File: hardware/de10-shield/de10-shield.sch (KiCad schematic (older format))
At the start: 35 parts, among them J1 GPIO_0, J10 SW3, J11 SW4, J12 SW5, J13 SW6, J14 SW7, J15 GPIO_0_AUX, J16 GPIO_1_AUX, J17 TFT_DISPLAY, J18 LED_0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

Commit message: done
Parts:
- removed J15: GPIO_0_AUX, Connector_PinSocket_2.54mm:PinSocket_1x20_P2.54mm_Vertical, symbol Connector:Conn_01x20_Female
- added H5, H6: MountingHole_Pad, MountingHole:MountingHole_3.2mm_M3_DIN965_Pad, symbol Mechanical:MountingHole_Pad
- added J15: ENCODER_0, Connector_PinSocket_2.54mm:PinSocket_1x05_P2.54mm_Vertical, symbol Connector:Conn_01x05_Female
- added J20: 5V, Connector_PinHeader_2.54mm:PinHeader_1x02_P2.54mm_Vertical, symbol Connector:Conn_01x02_Female
- added J21: 3.3V, Connector_PinHeader_2.54mm:PinHeader_1x02_P2.54mm_Vertical, symbol Connector:Conn_01x02_Female
- added J22: ENCODER_1, Connector_PinSocket_2.54mm:PinSocket_1x05_P2.54mm_Vertical, symbol Connector:Conn_01x05_Female
- added J23: ENCODER_2, Connector_PinSocket_2.54mm:PinSocket_1x05_P2.54mm_Vertical, symbol Connector:Conn_01x05_Female
- added J24: ENCODER_3, Connector_PinSocket_2.54mm:PinSocket_1x05_P2.54mm_Vertical, symbol Connector:Conn_01x05_Female
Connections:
- net +3V3: now also J15.1 (Pin_1), J21.2 (Pin_2), J22.1 (Pin_1), J23.1 (Pin_1), J24.1 (Pin_1); no longer J2.29 (Pin_29)
- net +5V: now also J20.2 (Pin_2); no longer J1.11 (Pin_11)
- net DIR_0: now also J1.10 (Pin_10); no longer J1.21 (Pin_21)
- net EN_0: now also J1.2 (Pin_2); no longer J1.13 (Pin_13)
- net GND: now also H5.1, J15.2 (Pin_2), J20.1 (Pin_1), J21.1 (Pin_1), J22.2 (Pin_2), J23.2 (Pin_2), J24.2 (Pin_2); no longer J1.12 (Pin_12), J1.30 (Pin_30), J16.15 (Pin_15), J16.6 (Pin_6), J2.12 (Pin_12), J2.30 (Pin_30)
- net MS1_0: now also J1.4 (Pin_4); no longer J1.15 (Pin_15)
- net MS2_0: now also J1.6 (Pin_6); no longer J1.17 (Pin_17)
- net STEP_0: now also J1.8 (Pin_8); no longer J1.19 (Pin_19)
- net VMEM: now also H6.1
- net I_3: now reaches J1.16 (Pin_16)
- net I_3: now also J24.5 (Pin_5)
- net B_3: now reaches J1.18 (Pin_18)
- net B_3: now also J24.4 (Pin_4)
- net A_3: now reaches J1.20 (Pin_20)
- net A_3: now also J24.3 (Pin_3)
- net I_2: now reaches J1.22 (Pin_22)
- net I_2: now also J23.5 (Pin_5)
- net B_2: now reaches J1.24 (Pin_24)
- net B_2: now also J23.4 (Pin_4)
- net A_2: now reaches J1.26 (Pin_26)
- net A_2: now also J23.3 (Pin_3)
- net I_1: now reaches J1.28 (Pin_28)
- net I_1: now also J22.5 (Pin_5)
- net B_1: now reaches J1.32 (Pin_32)
- net B_1: now also J22.4 (Pin_4)
- net A_1: now reaches J1.34 (Pin_34)
- net A_1: now also J22.3 (Pin_3)
- net I_0: now reaches J1.36 (Pin_36)
- net I_0: now also J15.5 (Pin_5)
- net B_0: now reaches J1.38 (Pin_38)
- net B_0: now also J15.4 (Pin_4)
- net A_0: now reaches J1.40 (Pin_40)
- net A_0: now also J15.3 (Pin_3)
- new net: J16.6 (Pin_6), J2.12 (Pin_12)
- new net: J16.15 (Pin_15), J2.30 (Pin_30)
- no-connect marks 2 -> 12

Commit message: done and ordered
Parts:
- added H7: MountingHole_Pad, MountingHole:MountingHole_3.2mm_M3_DIN965_Pad, symbol Mechanical:MountingHole_Pad
- C13, C14: footprint Capacitor_SMD:C_0603_1608Metric -> Capacitor_SMD:C_1210_3225Metric_Pad1.33x2.70mm_HandSolder
- C15: footprint Capacitor_SMD:C_0402_1005Metric -> Capacitor_SMD:C_0603_1608Metric_Pad1.08x0.95mm_HandSolder
- C16: footprint Capacitor_SMD:C_0402_1005Metric -> Capacitor_SMD:C_0805_2012Metric_Pad1.18x1.45mm_HandSolder
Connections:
- net GND: now also H7.1
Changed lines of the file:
@@
 F 0 "C16" H 4315 5546 50  0000 L CNN
 F 1 "0.1uF" H 4315 5455 50  0000 L CNN
-F 2 "Capacitor_SMD:C_0402_1005Metric" H 4238 5350 50  0001 C CNN
+F 2 "Capacitor_SMD:C_0805_2012Metric_Pad1.18x1.45mm_HandSolder" H 4238 5350 50  0001 C CNN
 F 3 "~" H 4200 5500 50  0001 C CNN
 	1    4200 5500
@@
 F 0 "C14" H 1815 4746 50  0000 L CNN
 F 1 "2.2uF" H 1815 4655 50  0000 L CNN
-F 2 "Capacitor_SMD:C_0603_1608Metric" H 1738 4550 50  0001 C CNN
+F 2 "Capacitor_SMD:C_1210_3225Metric_Pad1.33x2.70mm_HandSolder" H 1738 4550 50  0001 C CNN
 F 3 "~" H 1700 4700 50  0001 C CNN
 	1    1700 4700
@@
 F 0 "C13" H 1615 5546 50  0000 L CNN
 F 1 "2.2uF" H 1615 5455 50  0000 L CNN
-F 2 "Capacitor_SMD:C_0603_1608Metric" H 1538 5350 50  0001 C CNN
+F 2 "Capacitor_SMD:C_1210_3225Metric_Pad1.33x2.70mm_HandSolder" H 1538 5350 50  0001 C CNN
 F 3 "~" H 1500 5500 50  0001 C CNN
 	1    1500 5500
@@
 F 0 "C15" H 2615 6846 50  0000 L CNN
 F 1 "5600pF" H 2615 6755 50  0000 L CNN
-F 2 "Capacitor_SMD:C_0402_1005Metric" H 2538 6650 50  0001 C CNN
+F 2 "Capacitor_SMD:C_0603_1608Metric_Pad1.08x0.95mm_HandSolder" H 2538 6650 50  0001 C CNN
 F 3 "~" H 2500 6800 50  0001 C CNN
 	1    2500 6800
@@
 NoConn ~ 2550 3425
 NoConn ~ 4200 3425
+$Comp
+L Mechanical:MountingHole_Pad H7
+U 1 1 605964B9
+P 9950 3825
+F 0 "H7" H 10050 3874 50  0000 L CNN
+F 1 "MountingHole_Pad" H 10050 3783 50  0000 L CNN
+F 2 "MountingHole:MountingHole_3.2mm_M3_DIN965_Pad" H 9950 3825 50  0001 C CNN
+F 3 "~" H 9950 3825 50  0001 C CNN
+	1    9950 3825
+	1    0    0    -1
+$EndComp
+$Comp
+L power:GND #PWR0104
+U 1 1 605964BF
+P 9950 3925
+F 0 "#PWR0104" H 9950 3675 50  0001 C CNN
+F 1 "GND" V 9955 3797 50  0000 R CNN
+F 2 "" H 9950 3925 50  0001 C CNN
+F 3 "" H 9950 3925 50  0001 C CNN
+	1    9950 3925
+	0    1    1    0
+$EndComp
 $EndSCHEMATC

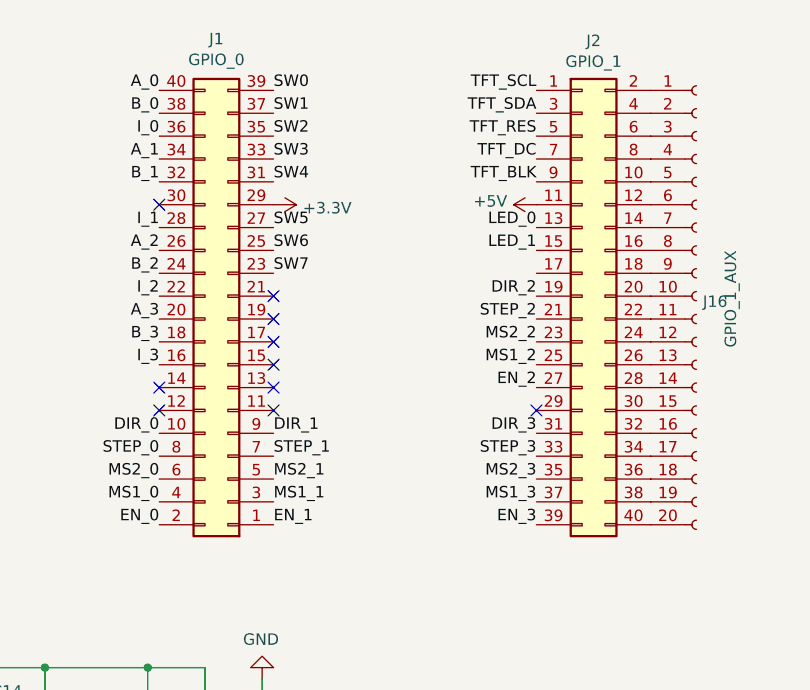
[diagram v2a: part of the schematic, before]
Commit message: with de10 shield pinout
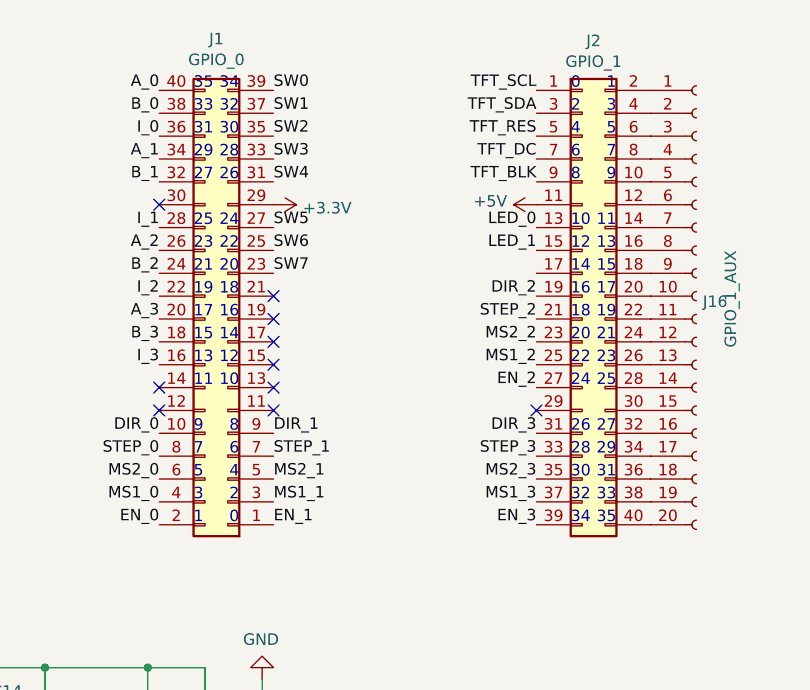
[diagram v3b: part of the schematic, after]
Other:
- note added: "0"
- note added: "1"
- note added: "10"
- note added: "11"
- note added: "12"
- note added: "13"
- note added: "14"
- note added: "15"
- note added: "16"
- note added: "17"
- note added: "18"
- note added: "19"
- note added: "2"
- note added: "20"
- note added: "21"
- note added: "22"
- note added: "23"
- note added: "24"
- note added: "25"
- note added: "26"
- note added: "27"
- note added: "28"
- note added: "29"
- note added: "3"
- note added: "30"
- note added: "31"
- note added: "32"
- note added: "33"
- note added: "34"
- note added: "35"
- note added: "4"
- note added: "5"
- note added: "6"
- note added: "7"
- note added: "8"
- note added: "9"
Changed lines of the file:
@@
 	0    1    1    0
 $EndComp
+Text Notes 4350 2025 0    50   ~ 0
+0
+Text Notes 4350 2125 0    50   ~ 0
+2
+Text Notes 4350 2225 0    50   ~ 0
+4
+Text Notes 4350 2325 0    50   ~ 0
+6
+Text Notes 4350 2425 0    50   ~ 0
+8
+Text Notes 4350 2625 0    50   ~ 0
+10
+Text Notes 4350 2725 0    50   ~ 0
+12
+Text Notes 4350 2825 0    50   ~ 0
+14
+Text Notes 4350 2925 0    50   ~ 0
+16
+Text Notes 4350 3025 0    50   ~ 0
+18
+Text Notes 4350 3125 0    50   ~ 0
+20
+Text Notes 4350 3225 0    50   ~ 0
+22
+Text Notes 4350 3325 0    50   ~ 0
+24
+Text Notes 4350 3525 0    50   ~ 0
+26
+Text Notes 4350 3625 0    50   ~ 0
+28
+Text Notes 4350 3725 0    50   ~ 0
+30
+Text Notes 4350 3825 0    50   ~ 0
+32
+Text Notes 4350 3925 0    50   ~ 0
+34
+Text Notes 4550 2025 2    50   ~ 0
+1
+Text Notes 4550 2125 2    50   ~ 0
+3
+Text Notes 4550 2225 2    50   ~ 0
+5
+Text Notes 4550 2325 2    50   ~ 0
+7
+Text Notes 4550 2425 2    50   ~ 0
+9
+Text Notes 4550 2625 2    50   ~ 0
+11
+Text Notes 4550 2725 2    50   ~ 0
+13
+Text Notes 4550 2825 2    50   ~ 0
+15
+Text Notes 4550 2925 2    50   ~ 0
+17
+Text Notes 4550 3025 2    50   ~ 0
+19
+Text Notes 4550 3125 2    50   ~ 0
+21
+Text Notes 4550 3225 2    50   ~ 0
+23
+Text Notes 4550 3325 2    50   ~ 0
+25
+Text Notes 4550 3525 2    50   ~ 0
+27
+Text Notes 4550 3625 2    50   ~ 0
+29
+Text Notes 4550 3725 2    50   ~ 0
+31
+Text Notes 4550 3825 2    50   ~ 0
+33
+Text Notes 4550 3925 2    50   ~ 0
+35
+Text Notes 2900 3925 2    50   ~ 0
+0
+Text Notes 2900 3825 2    50   ~ 0
+2
+Text Notes 2900 3725 2    50   ~ 0
+4
+Text Notes 2900 3625 2    50   ~ 0
+6
+Text Notes 2900 3525 2    50   ~ 0
+8
+Text Notes 2900 3325 2    50   ~ 0
+10
+Text Notes 2900 3225 2    50   ~ 0
+12
+Text Notes 2900 3125 2    50   ~ 0
+14
+Text Notes 2900 3025 2    50   ~ 0
+16
+Text Notes 2900 2925 2    50   ~ 0
+18
+Text Notes 2900 2825 2    50   ~ 0
+20
+Text Notes 2900 2725 2    50   ~ 0
+22
+Text Notes 2900 2625 2    50   ~ 0
+24
+Text Notes 2900 2425 2    50   ~ 0
+26
+Text Notes 2900 2325 2    50   ~ 0
+28
+Text Notes 2900 2225 2    50   ~ 0
+30
+Text Notes 2900 2125 2    50   ~ 0
+32
+Text Notes 2900 2025 2    50   ~ 0
+34
+Text Notes 2700 3925 0    50   ~ 0
+1
+Text Notes 2700 3825 0    50   ~ 0
+3
+Text Notes 2700 3725 0    50   ~ 0
+5
+Text Notes 2700 3625 0    50   ~ 0
+7
+Text Notes 2700 3525 0    50   ~ 0
+9
+Text Notes 2700 3325 0    50   ~ 0
+11
+Text Notes 2700 3225 0    50   ~ 0
+13
+Text Notes 2700 3125 0    50   ~ 0
+15
+Text Notes 2700 3025 0    50   ~ 0
+17
+Text Notes 2700 2925 0    50   ~ 0
+19
+Text Notes 2700 2825 0    50   ~ 0
+21
+Text Notes 2700 2725 0    50   ~ 0
+23
+Text Notes 2700 2625 0    50   ~ 0
+25
+Text Notes 2700 2425 0    50   ~ 0
+27
+Text Notes 2700 2325 0    50   ~ 0
+29
+Text Notes 2700 2225 0    50   ~ 0
+31
+Text Notes 2700 2125 0    50   ~ 0
+33
+Text Notes 2700 2025 0    50   ~ 0
+35
 $EndSCHEMATC
